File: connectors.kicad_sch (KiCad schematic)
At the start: 47 parts, among them CN901 HuCARD, CN902 JOY1, Q304 N/P

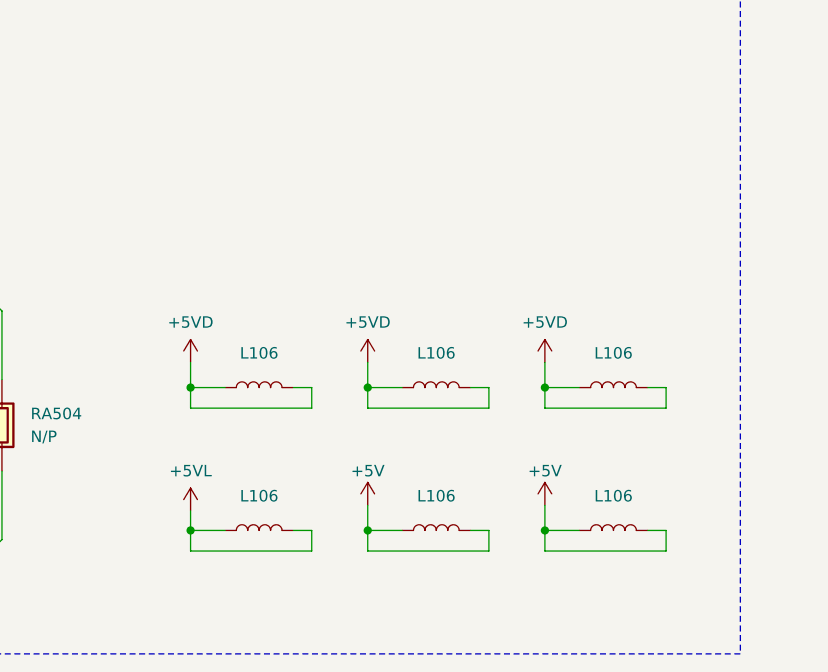
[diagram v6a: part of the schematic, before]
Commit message: BOM corrections, cosmetic PCB updates.
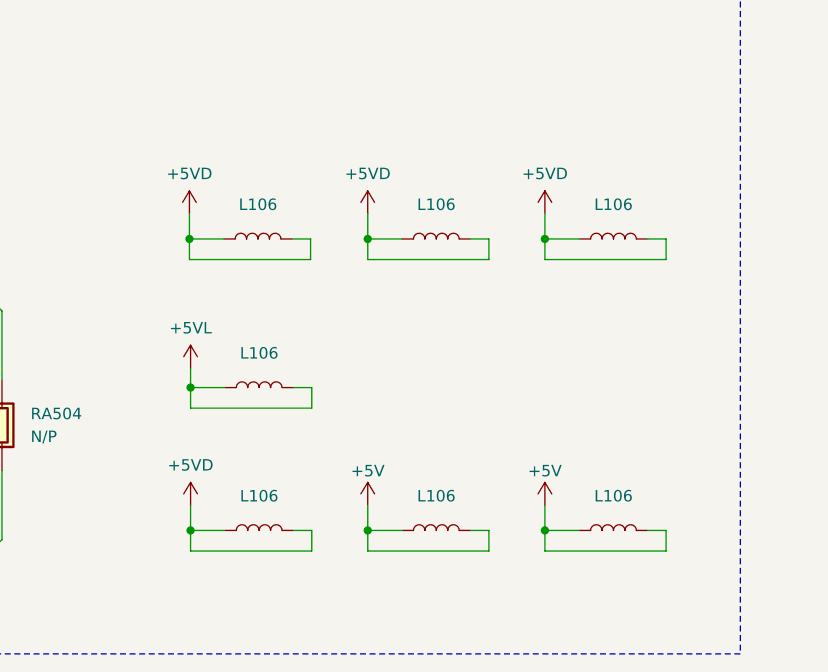
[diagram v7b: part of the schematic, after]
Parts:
- added L106: ~, A-PCENGINE:SMD_0805_Narrow, symbol Device:L
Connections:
- net +5VD: now also L106.1, L106.2
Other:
- moved on the sheet: L106

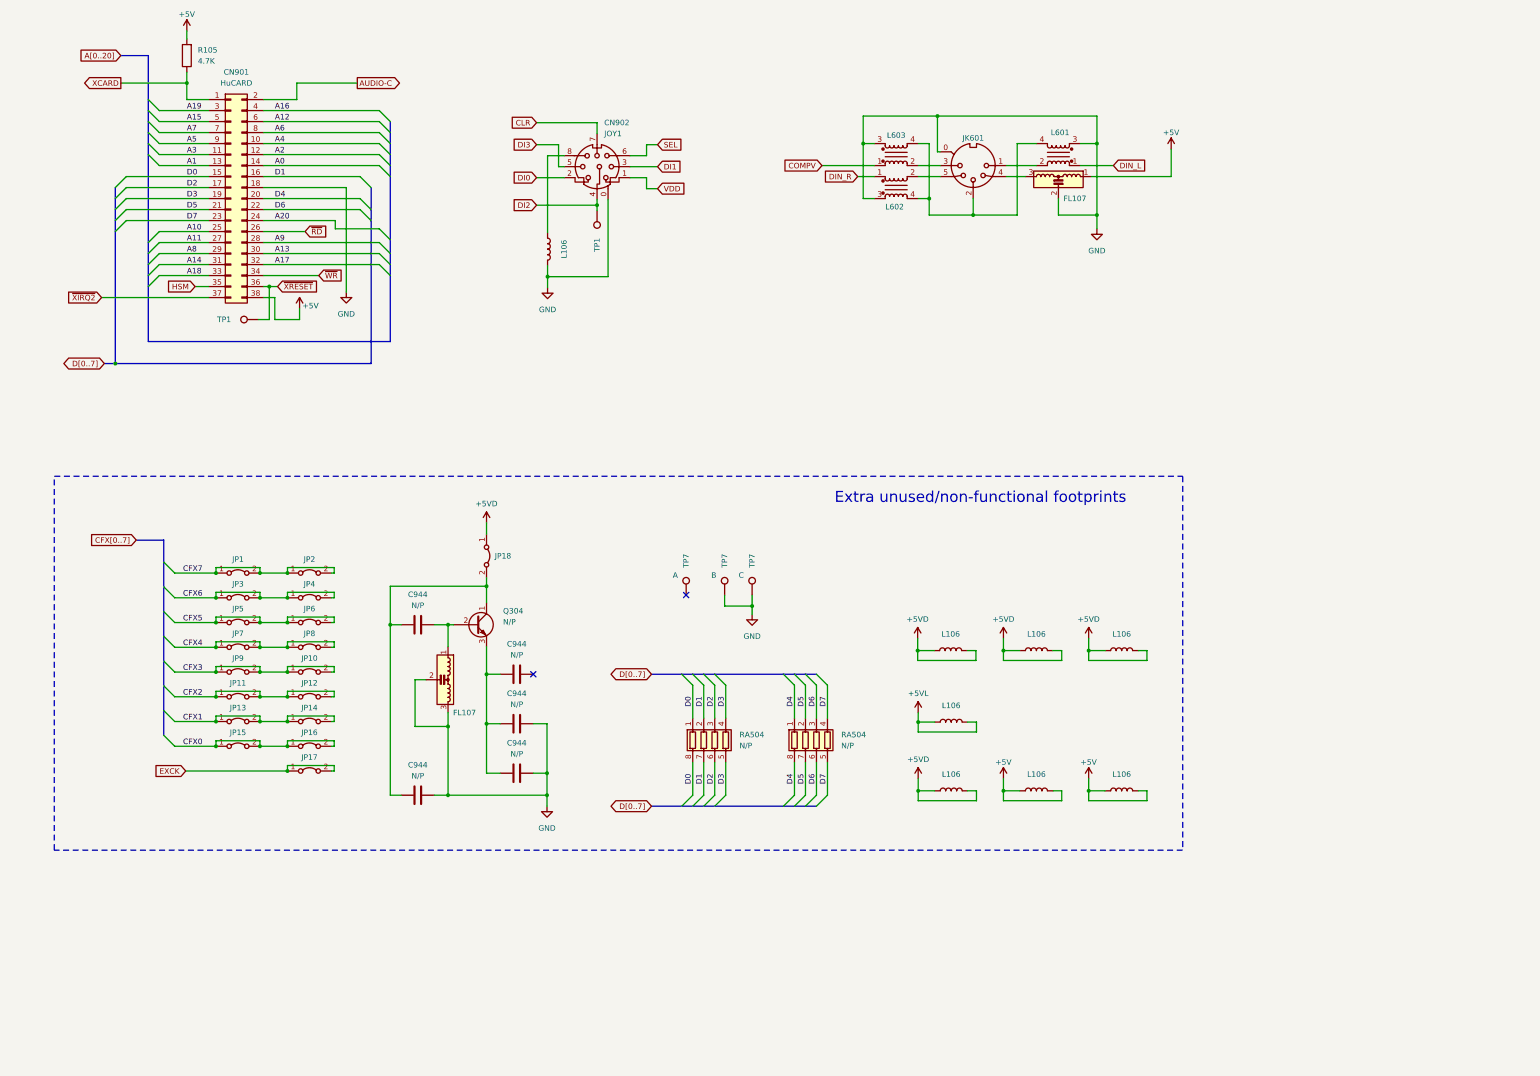
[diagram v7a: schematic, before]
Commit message: Add (excluded) HuCard slot for Turbo Duo to schematics.
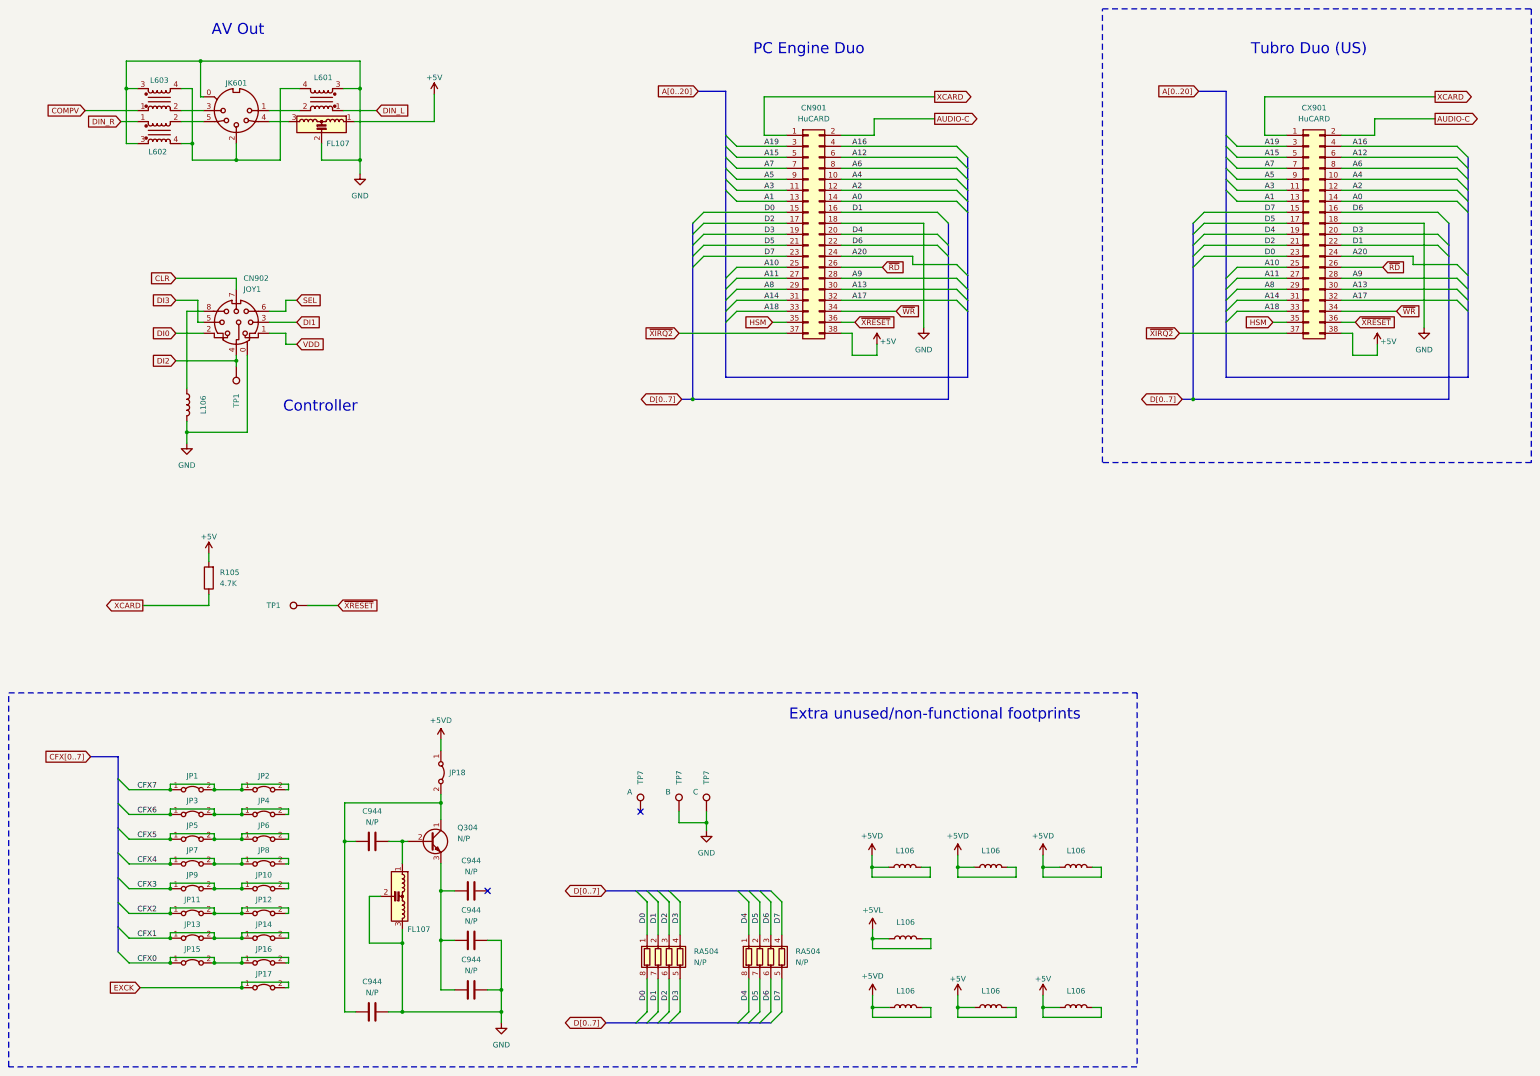
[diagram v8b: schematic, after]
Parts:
- added CX901: HuCARD, A-PCENGINE:Duo_HuCard, symbol Connector_Generic:Conn_02x19_Odd_Even
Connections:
- net +5V: now also CX901.38 (Pin_38)
- net A0: now also CX901.14 (Pin_14)
- net A1: now also CX901.13 (Pin_13)
- net A10: now also CX901.25 (Pin_25)
- net A11: now also CX901.27 (Pin_27)
- net A12: now also CX901.6 (Pin_6)
- net A13: now also CX901.30 (Pin_30)
- net A14: now also CX901.31 (Pin_31)
- net A15: now also CX901.5 (Pin_5)
- net A16: now also CX901.4 (Pin_4)
- net A17: now also CX901.32 (Pin_32)
- net A18: now also CX901.33 (Pin_33)
- net A19: now also CX901.3 (Pin_3)
- net A2: now also CX901.12 (Pin_12)
- net A20: now also CX901.24 (Pin_24)
- net A3: now also CX901.11 (Pin_11)
- net A4: now also CX901.10 (Pin_10)
- net A5: now also CX901.9 (Pin_9)
- net A6: now also CX901.8 (Pin_8)
- net A7: now also CX901.7 (Pin_7)
- net A8: now also CX901.29 (Pin_29)
- net A9: now also CX901.28 (Pin_28)
- net AUDIO-C: now also CX901.2 (Pin_2)
- net D0: now also CX901.23 (Pin_23)
- net D1: now also CX901.22 (Pin_22)
- net D2: now also CX901.21 (Pin_21)
- net D3: now also CX901.20 (Pin_20)
- net D4: now also CX901.19 (Pin_19)
- net D5: now also CX901.17 (Pin_17)
- net D6: now also CX901.16 (Pin_16)
- net D7: now also CX901.15 (Pin_15)
- net GND: now also CX901.18 (Pin_18)
- net HSM: now also CX901.35 (Pin_35)
- net XCARD: now also CX901.1 (Pin_1)
- net ~{RD}: now also CX901.26 (Pin_26)
- net ~{WR}: now also CX901.34 (Pin_34)
- net ~{XIRQ2}: now also CX901.37 (Pin_37)
- net ~{XRESET}: now also CX901.36 (Pin_36)
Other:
- note added: "AV Out"
- note added: "Controller"
- note added: "PC Engine Duo"
- note added: "Tubro Duo (US)"
- moved on the sheet: C944, CN901, CN902, FL107, JK601, JP1, JP10, JP11, JP12, JP13, JP14, JP15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
